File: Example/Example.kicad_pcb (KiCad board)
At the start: 2 copper layers, 50 x 45 mm, 5 parts, among them J1 Conn_01x03_Female, U1 PIC12C508A-ISN

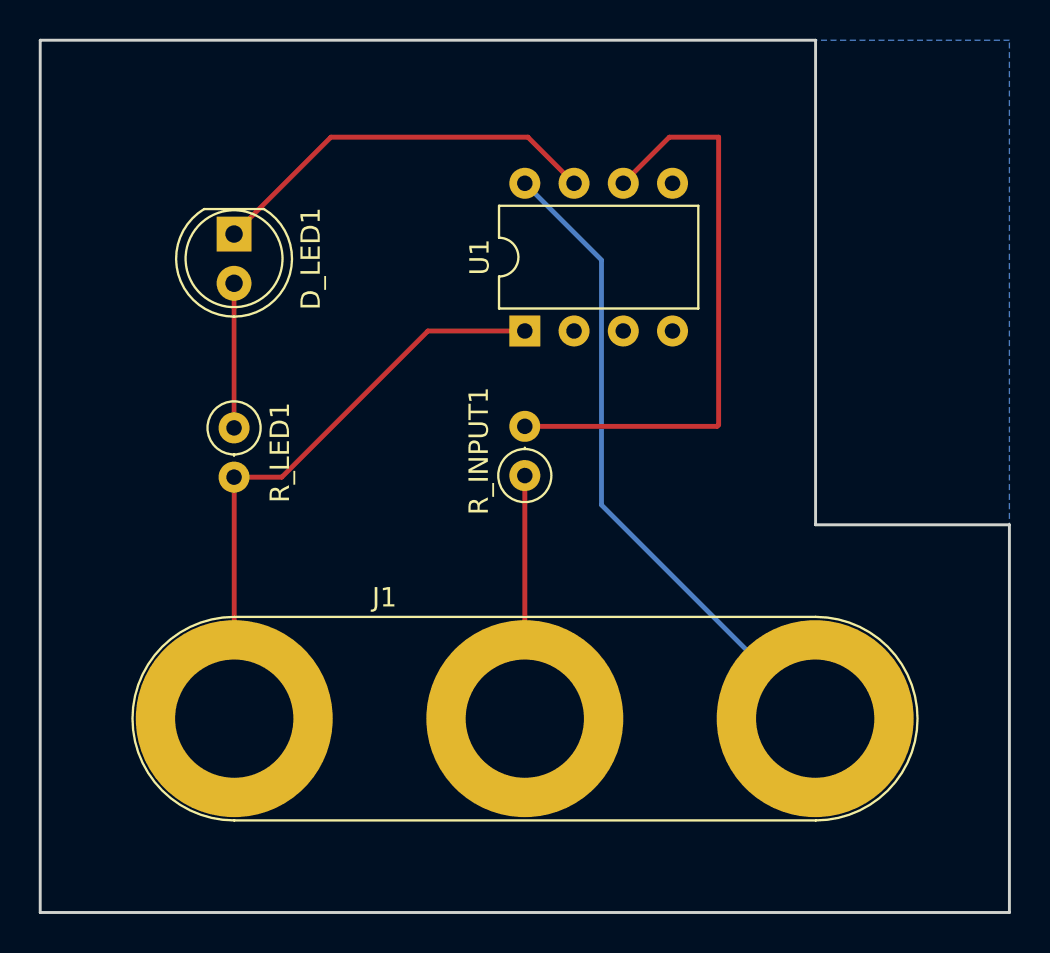
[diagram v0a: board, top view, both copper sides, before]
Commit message: Added missing ground plane
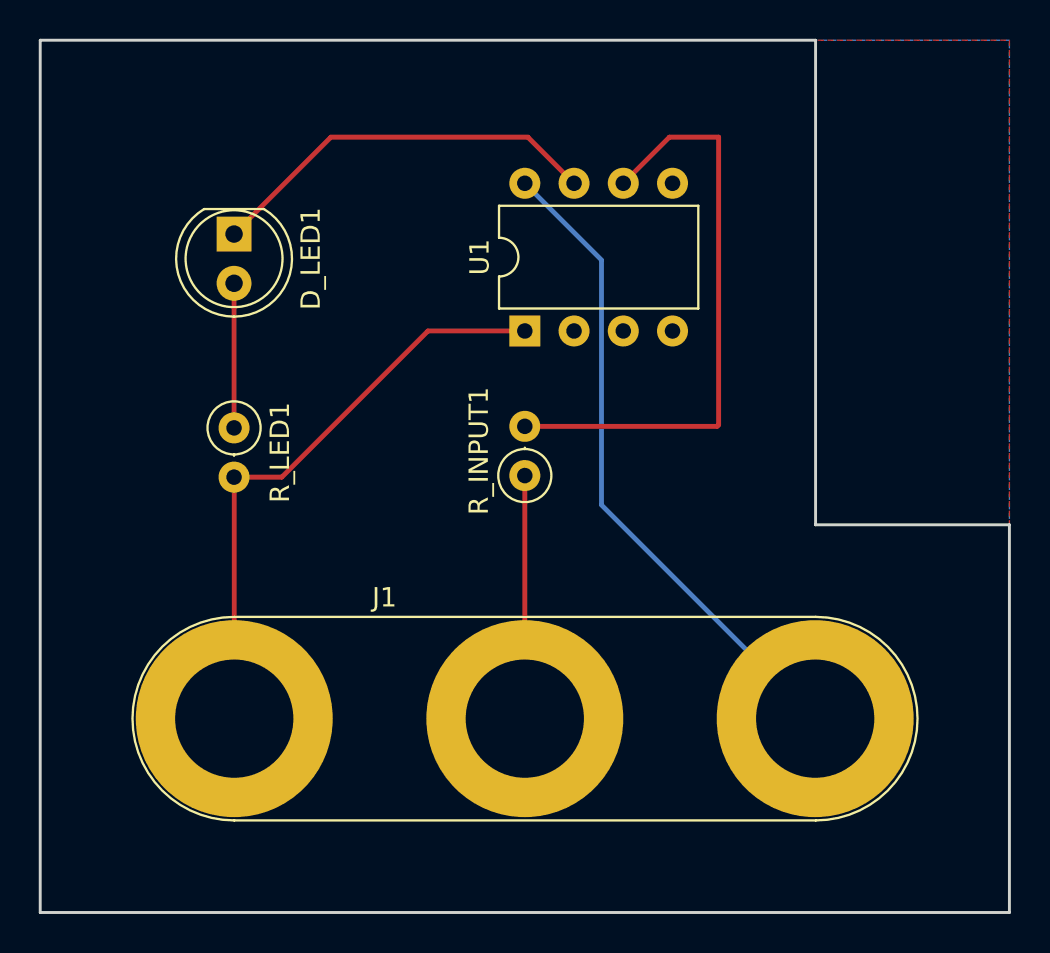
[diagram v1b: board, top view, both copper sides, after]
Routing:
- added copper zone on F.Cu, net GND
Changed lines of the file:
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@@
+    )
+  )
+  (zone (net 4) (net_name GND) (layer F.Cu) (hatch edge 0.508)
+    (connect_pads (clearance 0.508))
+    (min_thickness 0.254)
+    (fill yes (arc_segments 16) (thermal_gap 0.508) (thermal_bridge_width 0.508))
+    (polygon
+      (pts
+        (xy 170 90) (xy 170 135) (xy 120 135) (xy 120 90)
+      )
     )
   )
